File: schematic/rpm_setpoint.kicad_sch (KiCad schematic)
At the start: 1 part

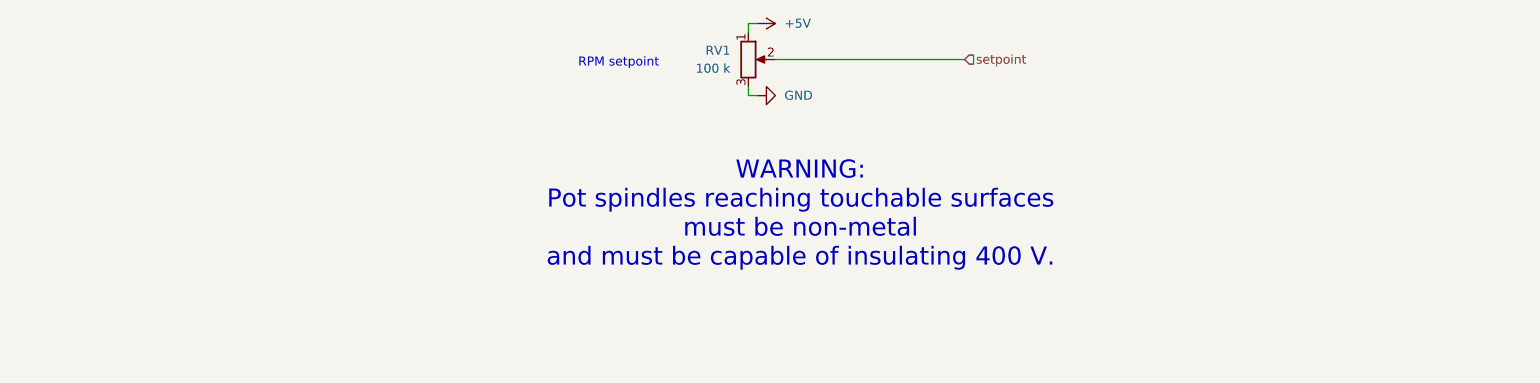
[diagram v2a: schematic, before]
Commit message: schematic: Update trig resistor
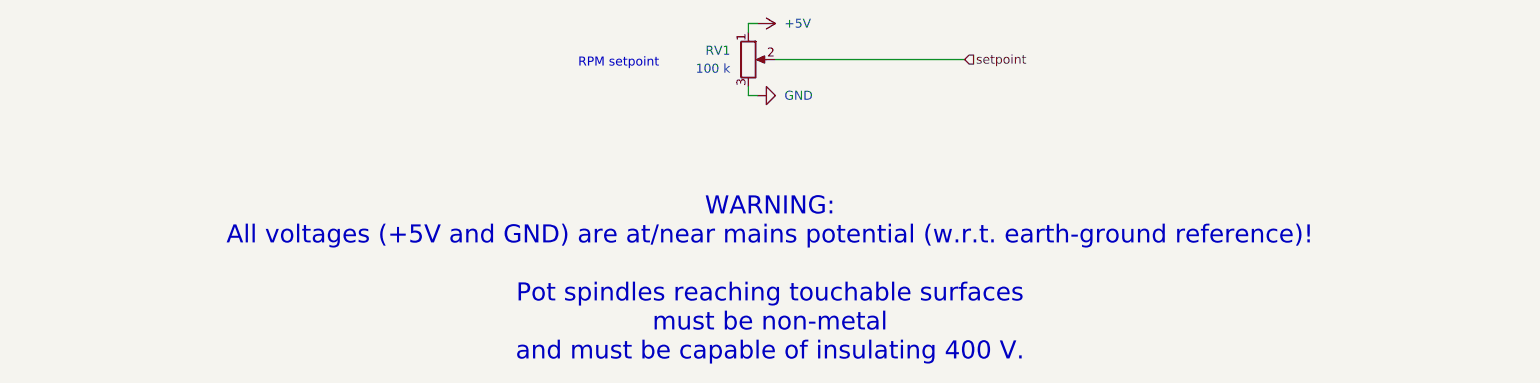
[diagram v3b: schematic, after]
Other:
- note added: "WARNING: All voltages (+5V and GND) are at/near mains potential (w.r.t. earth-ground reference)! Pot spindles reaching touchable surfaces must be non-metal and must be capable of insulating 400 V."
- note removed: "WARNING: Pot spindles reaching touchable surfaces must be non-metal and must be capable of insulating 400 V."
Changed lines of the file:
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@@
 		(company "Michael Büsch <m@bues.ch>")
 	)
-	(text "WARNING:\nPot spindles reaching touchable surfaces\nmust be non-metal\nand must be capable of insulating 400 V."
+	(text "WARNING:\nAll voltages (+5V and GND) are at/near mains potential (w.r.t. earth-ground reference)!\n\nPot spindles reaching touchable surfaces\nmust be non-metal\nand must be capable of insulating 400 V."
 		(exclude_from_sim no)
-		(at 149.606 109.474 0)
+		(at 145.288 118.618 0)
 		(effects
 			(font
